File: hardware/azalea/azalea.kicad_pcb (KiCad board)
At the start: 4 copper layers, 70.6 x 53.3 mm, 88 parts, among them J1 NEIGHBOR1, J2 NEIGHBOR2, J3 USB-MICRO-B-SHIELDED, J4 USB-MICRO-B-SHIELDED, J5 JTAG, J7 BONUS_ROW, SW1 DFU, SW2 RESET, U1 LPC4330FBD144, U2 W25Q16DV, U3 AP7333, U4 IP4220CZ6, U5 NX5P2553GV, X1 XTAL4PIN, X2 RTC_XTAL

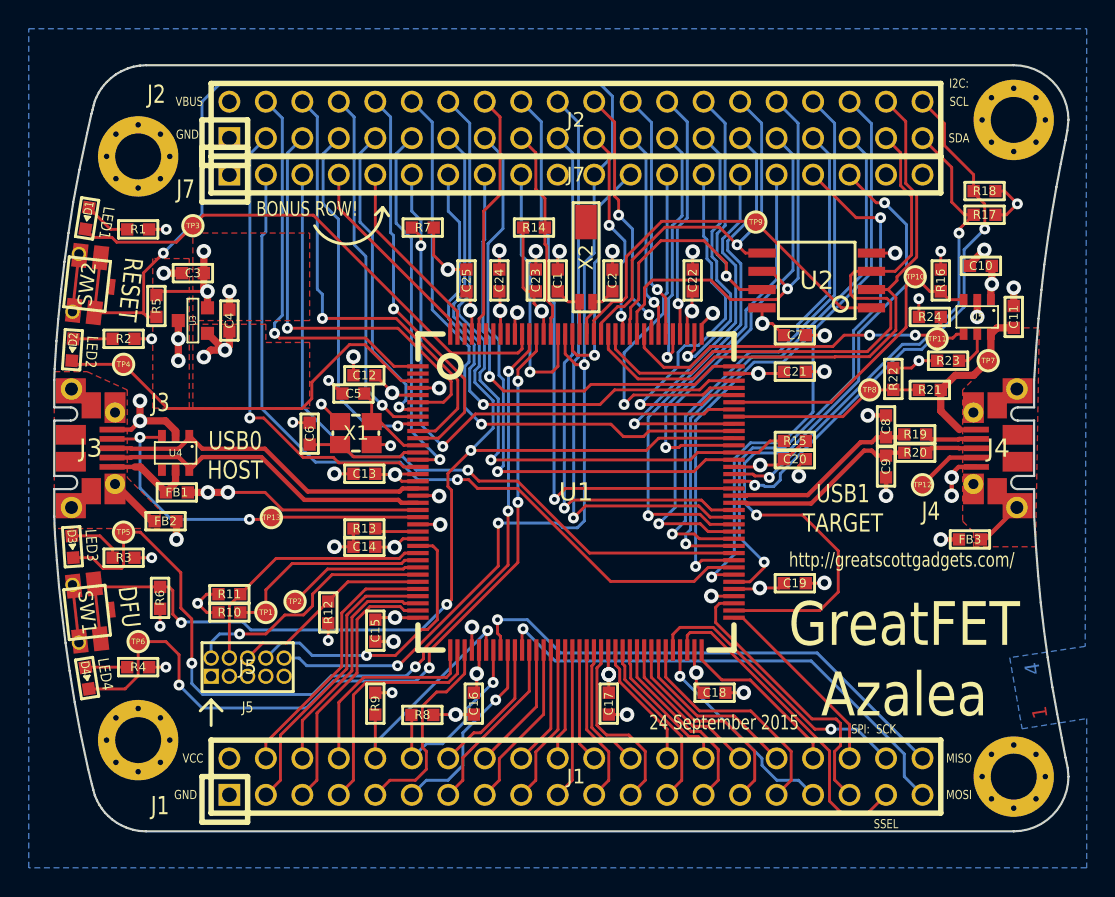
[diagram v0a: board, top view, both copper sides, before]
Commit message: daffodil: oops, J7 should not be DNP
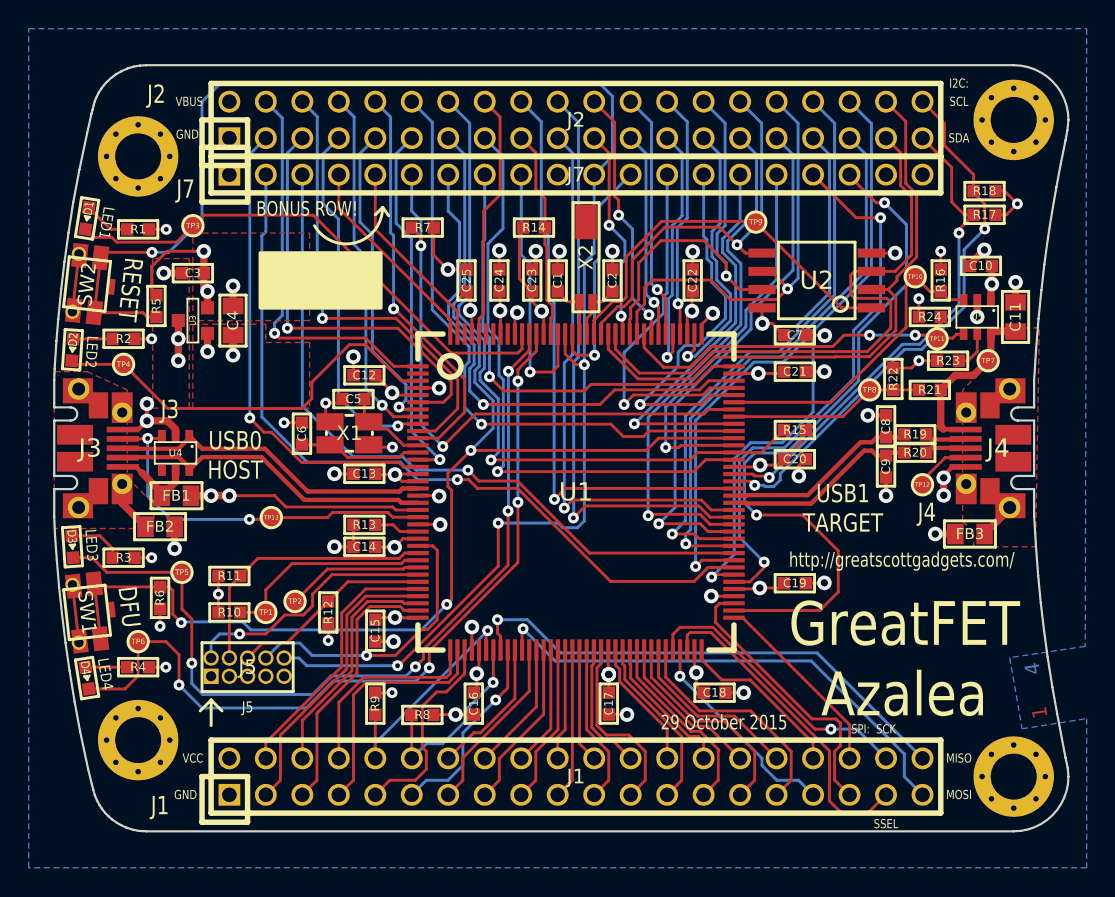
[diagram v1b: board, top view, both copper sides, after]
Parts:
- C11, C4, FB1, FB2, FB3: footprint gsg-modules:0603 -> gsg-modules:0805
- C8, C9: value 47pF -> 18pF
- J3, J4: footprint gsg-modules:USB-MICROB-FCI-10103592-EXT -> gsg-modules:USB-MICROB-FCI-10103592-LONGPADS
- X1: footprint gsg-modules:XTAL3.2x2.5mm -> gsg-modules:XTAL3.2x2.5mm-EXT
- moved TP5 4.93 mm to (114.8, 106.4)
- moved R11 1.27 mm to (118.1, 106.7)
- moved R15 0.76 mm to (157.5, 96.5)
- moved FB2 0.54 mm to (113.3, 103.3)
- moved C6 0.53 mm to (123.2, 96.8)
- moved X1 0.45 mm to (126.5, 96.7)
- moved C5 0.38 mm to (126.7, 94.4)
- moved FB3 0.38 mm to (169.7, 103.8)
- moved C4 0.25 mm to (118.4, 88.9)
- moved R13 0.25 mm to (127.5, 103.1)
- moved C23 0.25 mm to (139.2, 86.1)
- moved FB1 0.23 mm to (114.4, 101.1)
- moved C11 0.13 mm to (172.8, 88.6)
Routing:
- net /LED3: track 62.6 -> 59.2 mm
- net /VBUS: track 23.7 -> 21.2 mm
- net VCC: track 84.9 -> 86.9 mm
- net /USB0_ID: track 27.4 -> 26.6 mm
- net /TCK: track 18.3 -> 19.1 mm
- net /USB1_ID: track 4.53 -> 3.96 mm
- net Net-(C6-Pad1): track 8.02 -> 8.57 mm
- net /USB0_SHIELD: track 3.83 -> 3.30 mm
- net GND: track 81.1 -> 80.9 mm, vias 47 -> 46
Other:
- board text added: "29 October 2015"
- board text removed: "24 September 2015"
